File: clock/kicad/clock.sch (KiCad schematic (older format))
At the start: 111 parts, among them J1 USB-SS-52100-001, Q1 PN2222A, SW1 HOUR, SW2 MIN, SW3 TIME, U1 74HC4060, U10 74HC4511, U11 74HC4511, U12 74HC4511, U13 74HC4511, U14 KCSC02-105, U15 KCSC02-105, U16 KCSC02-105, U17 KCSC02-105, U18 KCSC02-105, U19 KCSC02-105, U2 SN74HC74N, U20 74HC14, U21 74HC157, U22 NE555P, U23 LD1117V, U3 74HC390, U4 74HC08, U5 74HC390, U6 74HC08, U7 74HC390, U8 74HC4511, U9 74HC4511

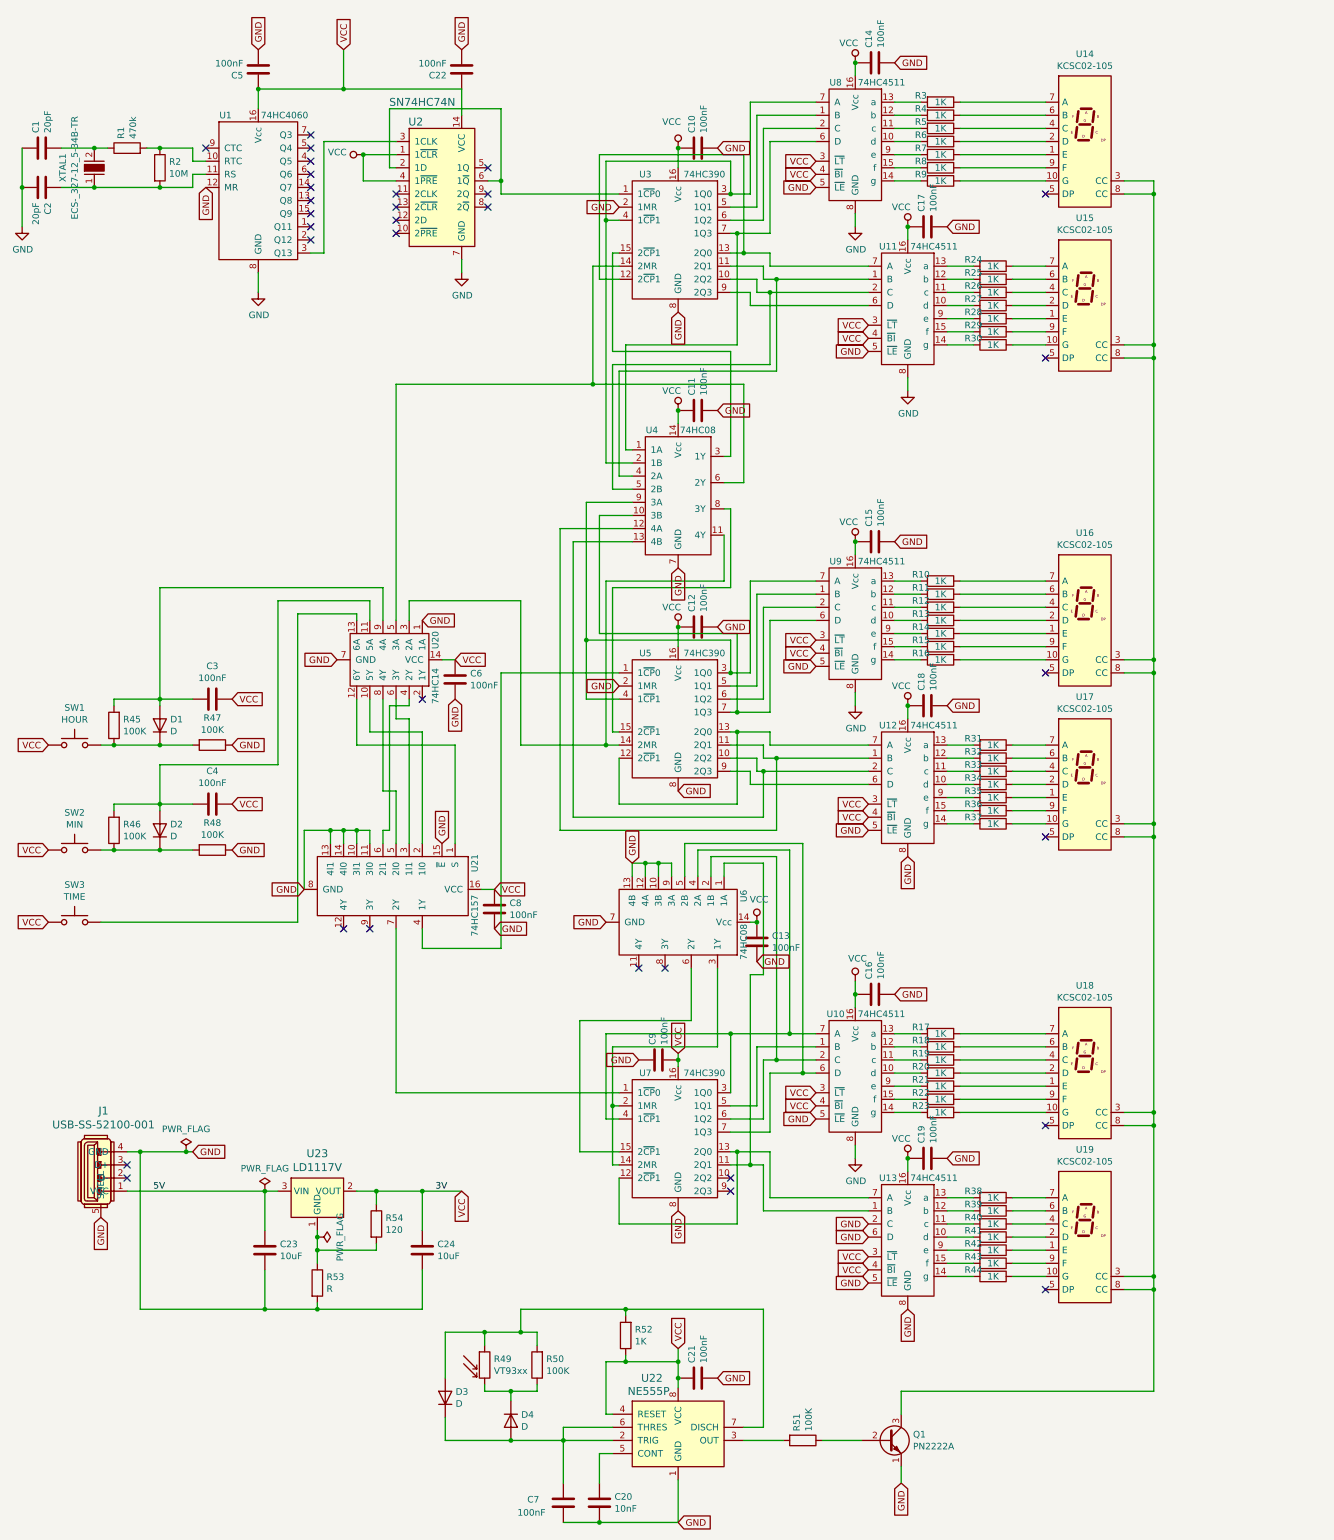
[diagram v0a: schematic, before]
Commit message: Clock: Added voltage regulator to PCB and switched to resistor networks.
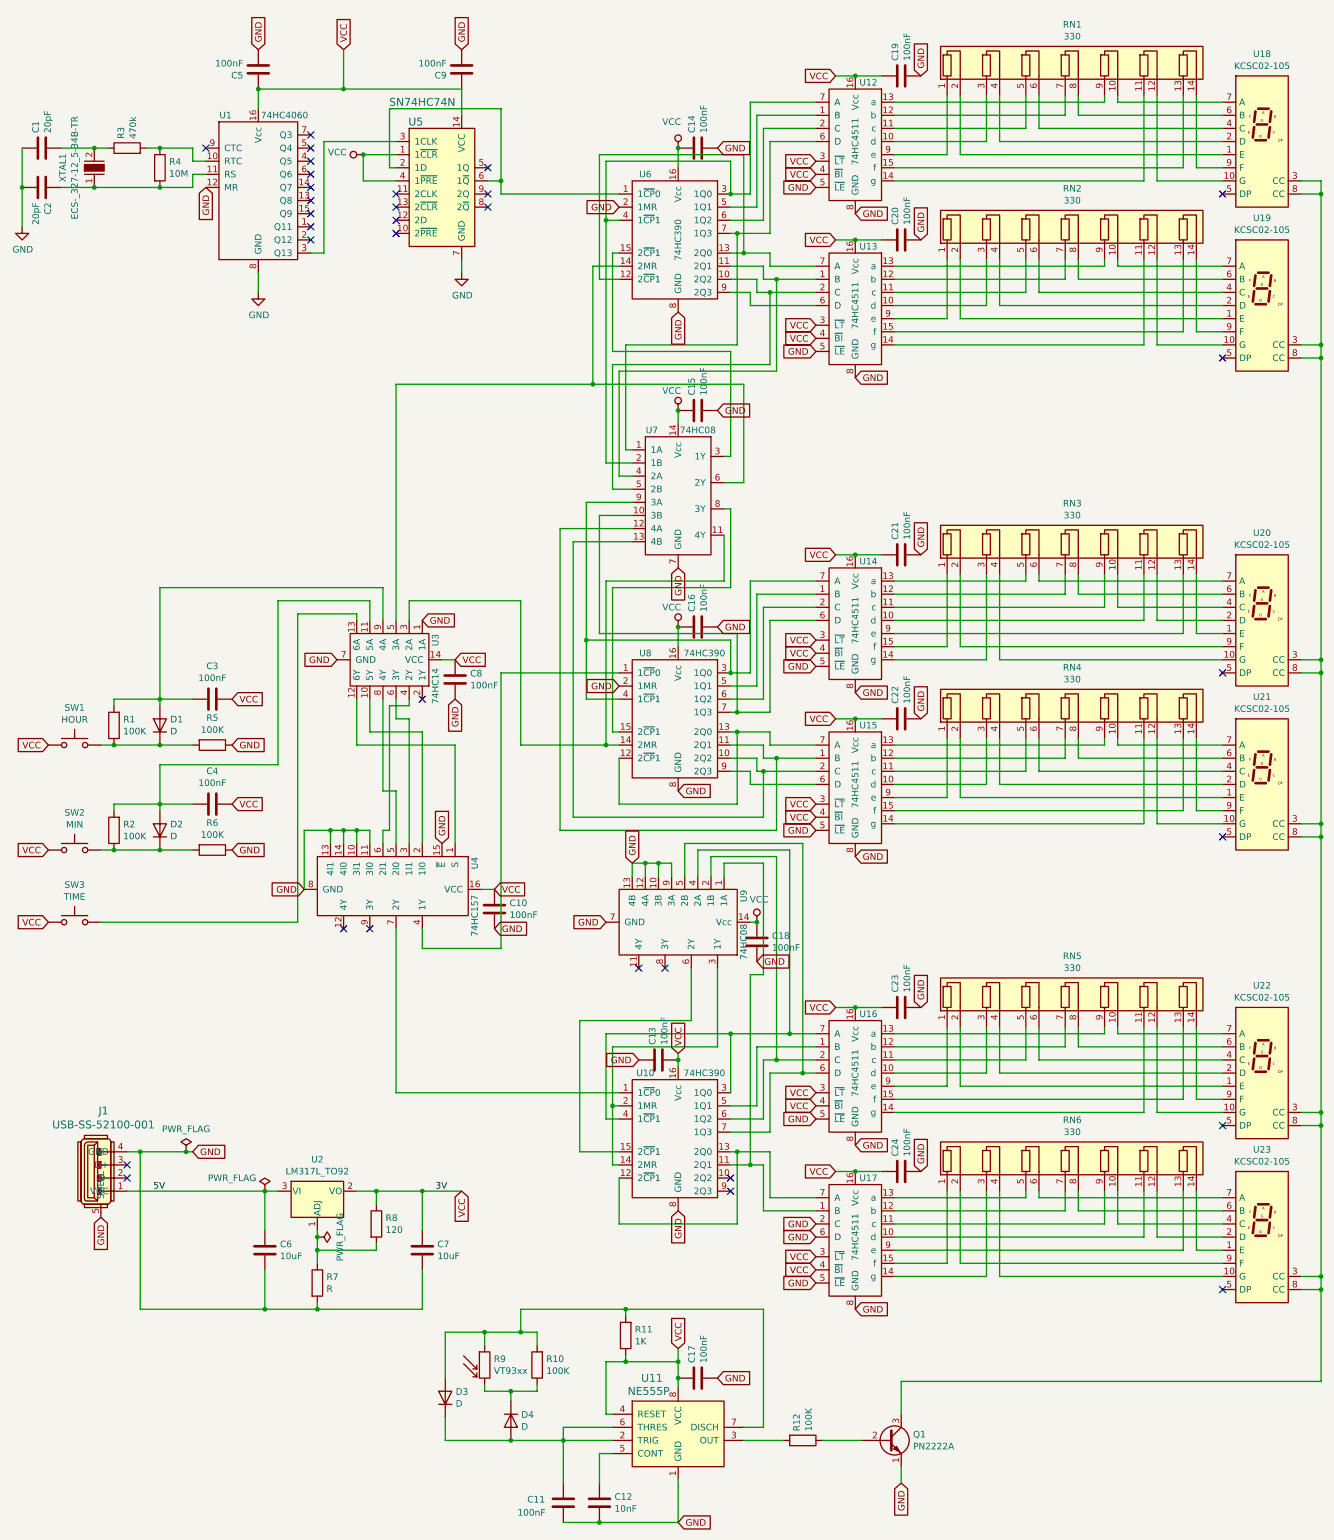
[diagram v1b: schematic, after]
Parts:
- removed R10, R11, R12, R13, R14, R15, R16, R17, R18, R19, R20, R21, R22, R23, R24, R25, R26, R27, R28, R29, R3, R30, R31, R32, R33, R34, R35, R36, R37, R38, R39, R4, R40, R41, R42, R43, R44, R5, R6, R7, R8, R9: 1K, Resistor_THT:R_Axial_DIN0207_L6.3mm_D2.5mm_P7.62mm_Horizontal, symbol Device:R
- removed U23: LD1117V, digikey-footprints:TO-220-3, symbol clock:LD1117V
- added RN1, RN2, RN3, RN4, RN5, RN6: 330, Resistor_THT:R_Array_SIP14, symbol Device:R_Pack07_SIP
- added U2: LM317L_TO92, Package_TO_SOT_THT:TO-92_Inline_Wide, symbol Regulator_Linear:LM317L_TO92
- C6: renamed from C23; footprint (none) -> Capacitor_THT:C_Disc_D5.0mm_W2.5mm_P2.50mm
- C7: renamed from C24; footprint (none) -> Capacitor_THT:C_Disc_D5.0mm_W2.5mm_P2.50mm
- R7: renamed from R53; footprint (none) -> Resistor_THT:R_Axial_DIN0207_L6.3mm_D2.5mm_P7.62mm_Horizontal
- R8: renamed from R54; footprint (none) -> Resistor_THT:R_Axial_DIN0207_L6.3mm_D2.5mm_P7.62mm_Horizontal
- renumbered C8 to C10, C7 to C11, C20 to C12, C9 to C13, C10 to C14, C11 to C15, C12 to C16, C21 to C17, C13 to C18, C14 to C19, C17 to C20, C15 to C21, C18 to C22, C16 to C23, C19 to C24, C6 to C8, C22 to C9, R45 to R1, R50 to R10, R52 to R11, R51 to R12, R46 to R2, R1 to R3, R2 to R4, R47 to R5, R48 to R6, R49 to R9, U7 to U10, U22 to U11, U8 to U12, U11 to U13, U9 to U14, U12 to U15, U10 to U16, U13 to U17, U14 to U18, U15 to U19, U16 to U20, U17 to U21, U18 to U22, U19 to U23, U20 to U3, U21 to U4, U2 to U5, U3 to U6, U4 to U7, U5 to U8, U6 to U9
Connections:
- net 5V: now also U2.3 (VI)
- net VCC: now also U2.2 (VO)
- net at U12.10 (d): now also RN1.3 (R2.1)
- net at U12.11 (c): now also RN1.5 (R3.1)
- net at U12.12 (b): now also RN1.7 (R4.1)
- net at U12.13 (a): now also RN1.9 (R5.1)
- net at U12.14 (g): now also RN1.11 (R6.1)
- net at U12.15 (f): now also RN1.13 (R7.1)
- net at U12.9 (e): now also RN1.1 (R1.1)
- net at U13.10 (d): now also RN2.3 (R2.1)
- net at U13.11 (c): now also RN2.5 (R3.1)
- net at U13.12 (b): now also RN2.7 (R4.1)
- net at U13.13 (a): now also RN2.9 (R5.1)
- net at U13.14 (g): now also RN2.11 (R6.1)
- net at U13.15 (f): now also RN2.13 (R7.1)
- net at U13.9 (e): now also RN2.1 (R1.1)
- net at U18.7 (A): now also RN1.10 (R5.2)
- net at U18.6 (B): now also RN1.8 (R4.2)
- net at U18.4 (C): now also RN1.6 (R3.2)
- net at U18.2 (D): now also RN1.4 (R2.2)
- net at U18.1 (E): now also RN1.2 (R1.2)
- net at U18.9 (F): now also RN1.14 (R7.2)
- net at U18.10 (G): now also RN1.12 (R6.2)
- net at U19.7 (A): now also RN2.10 (R5.2)
- net at U19.6 (B): now also RN2.8 (R4.2)
- net at U19.4 (C): now also RN2.6 (R3.2)
- net at U19.2 (D): now also RN2.4 (R2.2)
- net at U19.1 (E): now also RN2.2 (R1.2)
- net at U19.9 (F): now also RN2.14 (R7.2)
- net at U19.10 (G): now also RN2.12 (R6.2)
- net at U14.10 (d): now also RN3.11 (R6.1)
- net at U14.11 (c): now also RN3.9 (R5.1)
- net at U14.12 (b): now also RN3.7 (R4.1)
- net at U14.13 (a): now also RN3.5 (R3.1)
- net at U14.14 (g): now also RN3.3 (R2.1)
- net at U14.15 (f): now also RN3.1 (R1.1)
- net at U14.9 (e): now also RN3.13 (R7.1)
- net at U15.10 (d): now also RN4.3 (R2.1)
- net at U15.11 (c): now also RN4.5 (R3.1)
- net at U15.12 (b): now also RN4.7 (R4.1)
- net at U15.13 (a): now also RN4.9 (R5.1)
- net at U15.14 (g): now also RN4.11 (R6.1)
- net at U15.15 (f): now also RN4.13 (R7.1)
- net at U15.9 (e): now also RN4.1 (R1.1)
- net at U20.7 (A): now also RN3.6 (R3.2)
- net at U20.6 (B): now also RN3.8 (R4.2)
- net at U20.4 (C): now also RN3.10 (R5.2)
- net at U20.2 (D): now also RN3.12 (R6.2)
- net at U20.1 (E): now also RN3.14 (R7.2)
- net at U20.9 (F): now also RN3.2 (R1.2)
- net at U20.10 (G): now also RN3.4 (R2.2)
- net at U21.7 (A): now also RN4.10 (R5.2)
- net at U21.6 (B): now also RN4.8 (R4.2)
- net at U21.4 (C): now also RN4.6 (R3.2)
- net at U21.2 (D): now also RN4.4 (R2.2)
- net at U21.1 (E): now also RN4.2 (R1.2)
- net at U21.9 (F): now also RN4.14 (R7.2)
- net at U21.10 (G): now also RN4.12 (R6.2)
- net at U16.10 (d): now also RN5.3 (R2.1)
- net at U16.11 (c): now also RN5.5 (R3.1)
- net at U16.12 (b): now also RN5.7 (R4.1)
- net at U16.13 (a): now also RN5.9 (R5.1)
- net at U16.14 (g): now also RN5.11 (R6.1)
- net at U16.15 (f): now also RN5.13 (R7.1)
- net at U16.9 (e): now also RN5.1 (R1.1)
- net at U17.10 (d): now also RN6.11 (R6.1)
- net at U17.11 (c): now also RN6.9 (R5.1)
- net at U17.12 (b): now also RN6.7 (R4.1)
- net at U17.13 (a): now also RN6.5 (R3.1)
- net at U17.14 (g): now also RN6.3 (R2.1)
- net at U17.15 (f): now also RN6.1 (R1.1)
- net at U17.9 (e): now also RN6.13 (R7.1)
- net at U22.7 (A): now also RN5.10 (R5.2)
- net at U22.6 (B): now also RN5.8 (R4.2)
- net at U22.4 (C): now also RN5.6 (R3.2)
- net at U22.2 (D): now also RN5.4 (R2.2)
- net at U22.1 (E): now also RN5.2 (R1.2)
- net at U22.9 (F): now also RN5.14 (R7.2)
- net at U22.10 (G): now also RN5.12 (R6.2)
- net at U23.7 (A): now also RN6.6 (R3.2)
- net at U23.6 (B): now also RN6.8 (R4.2)
- net at U23.4 (C): now also RN6.10 (R5.2)
- net at U23.2 (D): now also RN6.12 (R6.2)
- net at U23.1 (E): now also RN6.14 (R7.2)
- net at U23.9 (F): now also RN6.2 (R1.2)
- net at U23.10 (G): now also RN6.4 (R2.2)
- net at R7.1, R8.2: now also U2.1 (ADJ)
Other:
- moved on the sheet: C19, C20, C21, C22, C23, C24, U13, U15, U17, U18, U19, U20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

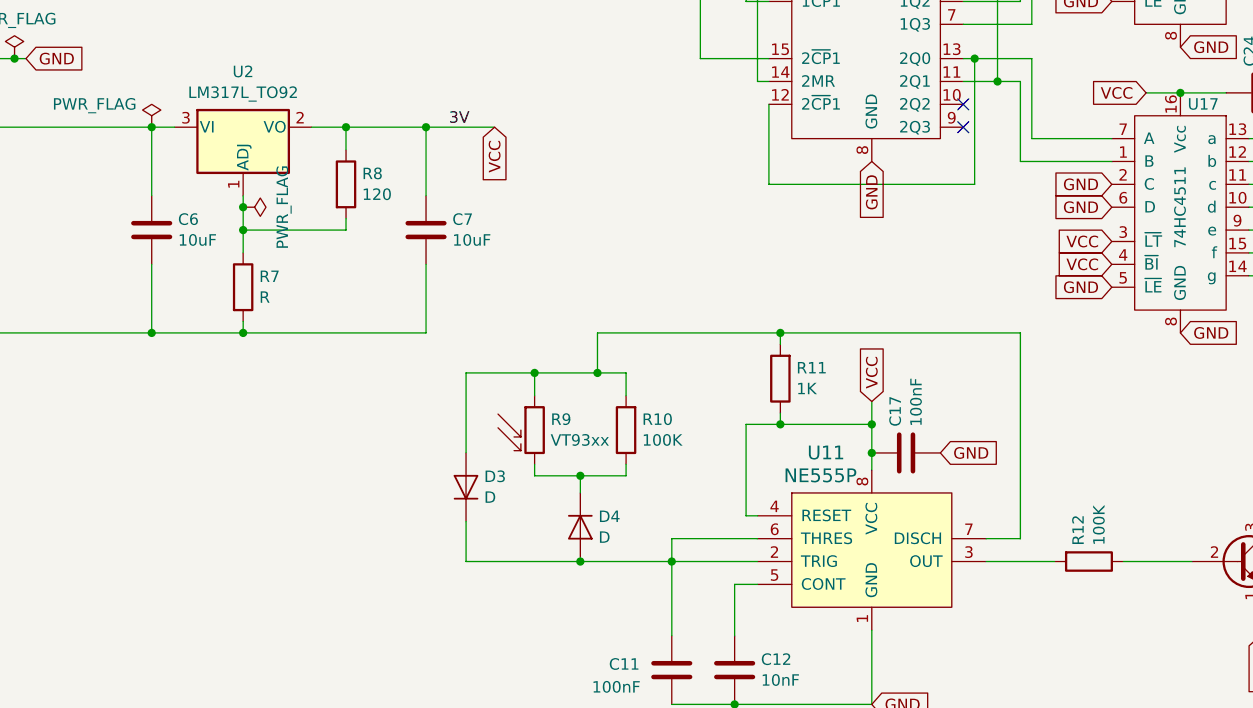
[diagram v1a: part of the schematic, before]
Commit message: Clock: Using a 500Ohm trimpot to tune the voltage regulator.
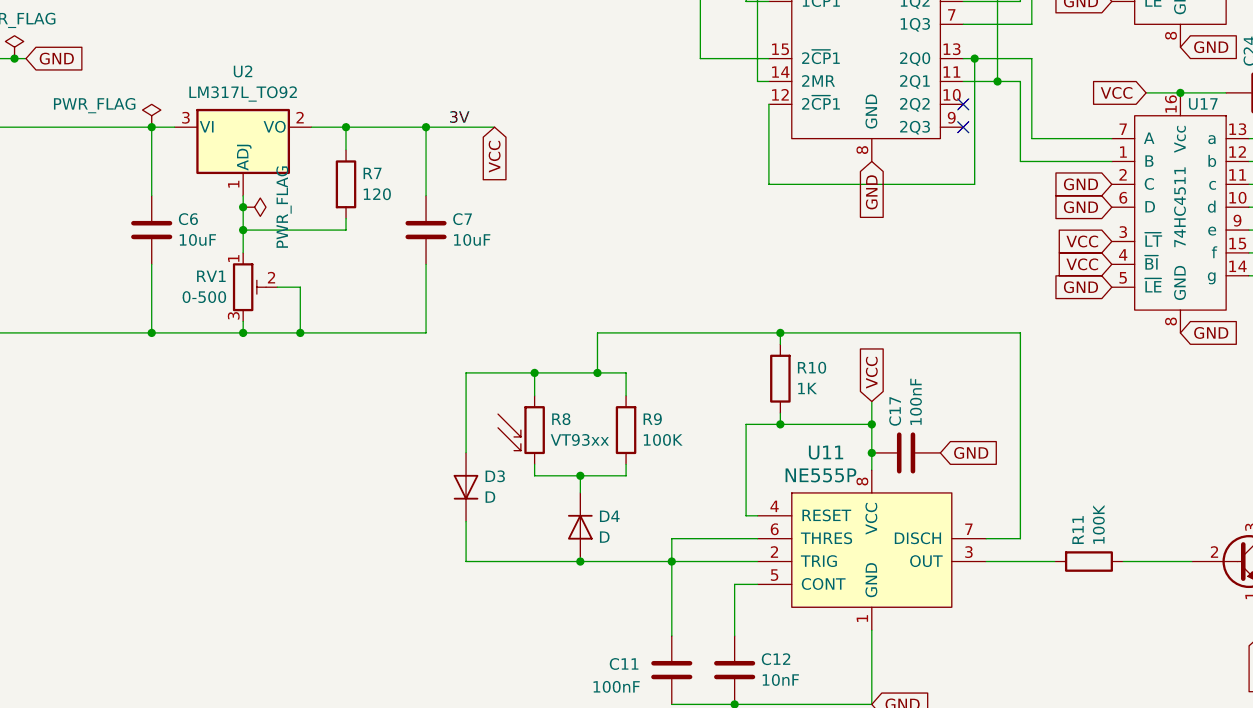
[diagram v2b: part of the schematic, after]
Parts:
- removed R7: R, Resistor_THT:R_Axial_DIN0207_L6.3mm_D2.5mm_P7.62mm_Horizontal, symbol Device:R
- added RV1: 0-500, Potentiometer_THT:Potentiometer_Bourns_3339P_Vertical_HandSoldering, symbol Device:R_POT_TRIM
- renumbered R11 to R10, R12 to R11, R8 to R7, R9 to R8, R10 to R9
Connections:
- net GND: now also RV1.2, RV1.3
- net at R7.2, U2.1 (ADJ): now also RV1.1
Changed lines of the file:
@@
 $EndComp
 $Comp
-L Device:R R10
+L Device:R R9
 U 1 1 5DB7BBEA
 P 4675 10775
-F 0 "R10" H 4605 10729 50  0000 R CNN
+F 0 "R9" H 4605 10729 50  0000 R CNN
 F 1 "100K" H 4605 10820 50  0000 R CNN
 F 2 "Resistor_THT:R_Axial_DIN0207_L6.3mm_D2.5mm_P7.62mm_Horizontal" V 4605 10775 50  0001 C CNN
@@
 	3975 10525 4275 10525
 $Comp
-L Sensor_Optical:VT93xx R9
+L Sensor_Optical:VT93xx R8
 U 1 1 5DC80BDF
 P 4275 10775
-F 0 "R9" H 4345 10821 50  0000 L CNN
+F 0 "R8" H 4345 10821 50  0000 L CNN
 F 1 "VT93xx" H 4345 10730 50  0000 L CNN
 F 2 "OptoDevice:R_LDR_4.9x4.2mm_P2.54mm_Vertical" V 4450 10775 50  0001 C CNN
@@
 	6250 11350 6550 11350
 $Comp
-L Device:R R12
+L Device:R R11
 U 1 1 5DEB054B
 P 6700 11350
-F 0 "R12" H 6630 11304 50  0000 R CNN
+F 0 "R11" H 6630 11304 50  0000 R CNN
 F 1 "100K" H 6630 11395 50  0000 R CNN
 F 2 "Resistor_THT:R_Axial_DIN0207_L6.3mm_D2.5mm_P7.62mm_Horizontal" V 6630 11350 50  0001 C CNN
@@
 	7450 11550 7450 11675
 $Comp
-L Device:R R11
+L Device:R R10
 U 1 1 5E34B6A6
 P 5350 10550
-F 0 "R11" H 5280 10504 50  0000 R CNN
+F 0 "R10" H 5280 10504 50  0000 R CNN
 F 1 "1K" H 5280 10595 50  0000 R CNN
 F 2 "Resistor_THT:R_Axial_DIN0207_L6.3mm_D2.5mm_P7.62mm_Horizontal" V 5280 10550 50  0001 C CNN
@@
 	1550 9150 1650 9150
 $Comp
-L Device:R R8
+L Device:R R7
 U 1 1 5DA44C3B
 P 3450 9700
-F 0 "R8" H 3520 9746 50  0000 L CNN
+F 0 "R7" H 3520 9746 50  0000 L CNN
 F 1 "120" H 3520 9655 50  0000 L CNN
 F 2 "Resistor_THT:R_Axial_DIN0207_L6.3mm_D2.5mm_P7.62mm_Horizontal" V 3380 9700 50  0001 C CNN
 F 3 "~" H 3450 9700 50  0001 C CNN
 	1    3450 9700
-	1    0    0    -1
-$EndComp
-$Comp
-L Device:R R7
-U 1 1 5DA450EA
-P 3000 10150
-F 0 "R7" H 3070 10196 50  0000 L CNN
-F 1 "R" H 3070 10105 50  0000 L CNN
-F 2 "Resistor_THT:R_Axial_DIN0207_L6.3mm_D2.5mm_P7.62mm_Horizontal" V 2930 10150 50  0001 C CNN
-F 3 "~" H 3000 10150 50  0001 C CNN
-	1    3000 10150
 	1    0    0    -1
 $EndComp
@@
 	3800 10050 3800 10350
 Wire Wire Line
-	3800 10350 3000 10350
+	3800 10350 3250 10350
 Wire Wire Line
 	1650 10350 1650 9150
@@
 Wire Wire Line
 	7900 10000 9900 10000
+$Comp
+L Device:R_POT_TRIM RV1
+U 1 1 610D8243
+P 3000 10150
+F 0 "RV1" H 2930 10196 50  0000 R CNN
+F 1 "0-500" H 2930 10105 50  0000 R CNN
+F 2 "Potentiometer_THT:Potentiometer_Bourns_3339P_Vertical_HandSoldering" H 3000 10150 50  0001 C CNN
+F 3 "~" H 3000 10150 50  0001 C CNN
+	1    3000 10150
+	1    0    0    -1
+$EndComp
+Wire Wire Line
+	3150 10150 3250 10150
+Wire Wire Line
+	3250 10150 3250 10350
+Connection ~ 3250 10350
+Wire Wire Line
+	3250 10350 3000 10350
 $EndSCHEMATC
